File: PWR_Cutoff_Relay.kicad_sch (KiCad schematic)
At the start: 7 parts, among them K1 RAYEX-L90AS, Q1 Q_NMOS_GSD

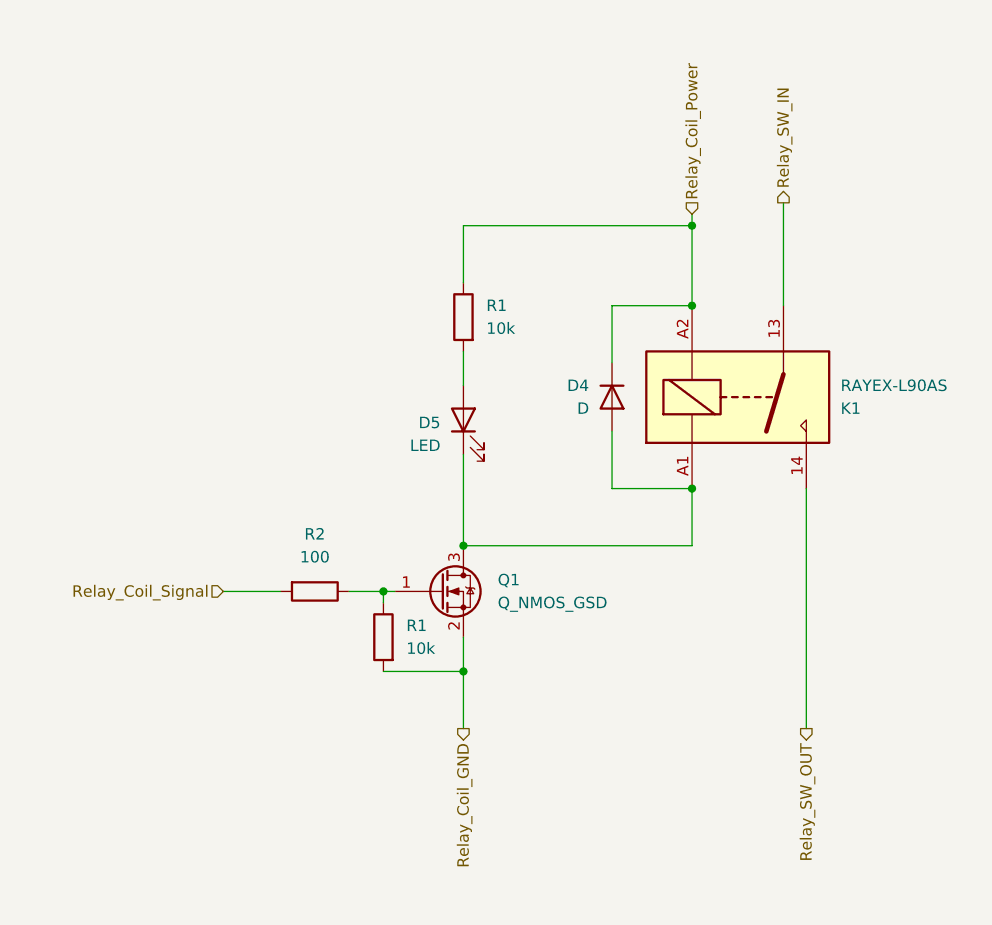
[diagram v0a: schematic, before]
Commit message: add switch, EMS & MCU
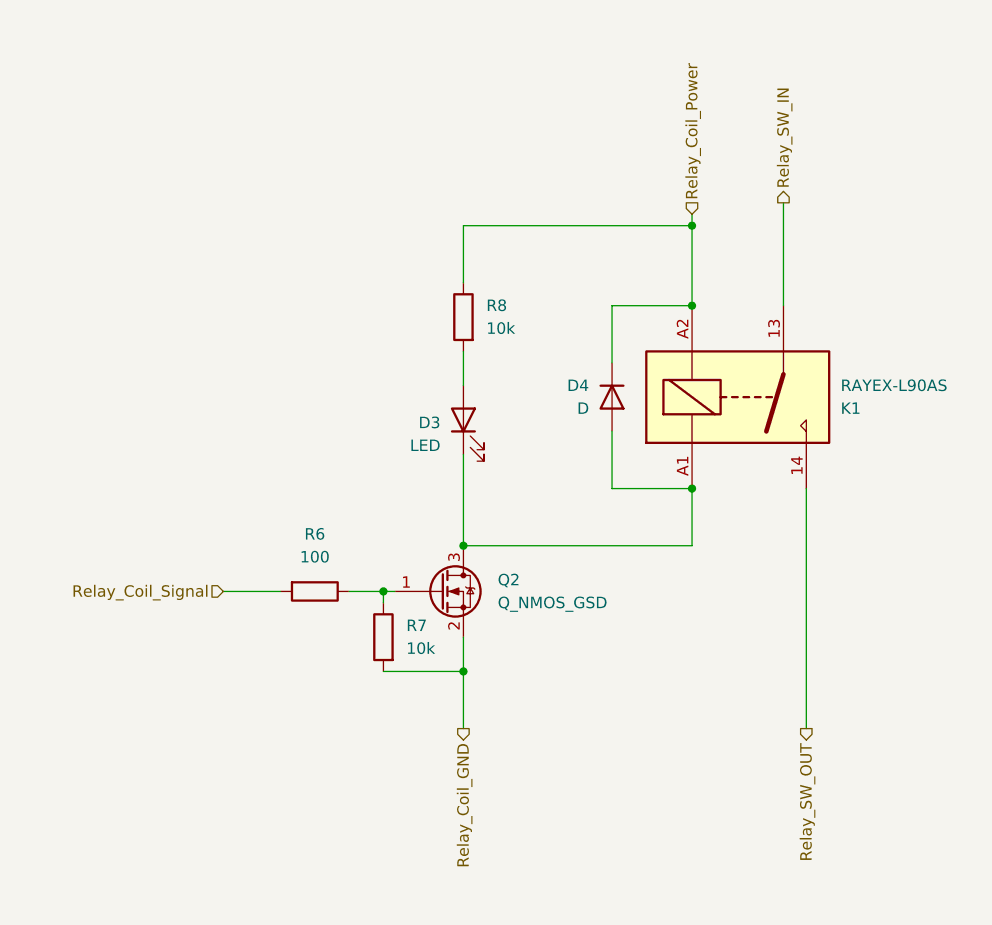
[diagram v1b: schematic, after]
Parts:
- renumbered D5 to D3, Q1 to Q2, R2 to R6, R1 to R7, R1 to R8
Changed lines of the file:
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@@
   (symbol (lib_id "Device:LED") (at 83.82 78.74 90) (unit 1)
     (in_bom yes) (on_board yes) (dnp no)
-    (property "Reference" "D5" (at 81.28 79.0575 90)
+    (property "Reference" "D3" (at 81.28 79.0575 90)
       (effects (font (size 1.27 1.27)) (justify left))
     )
@@
       (project "schematic_PWRcutoff"
         (path "/9e89b938-308a-42c1-b814-ac47b1ea682c/41c12bc5-ee22-4bb8-97ee-b610ccf60040"
-          (reference "D5") (unit 1)
+          (reference "D3") (unit 1)
         )
         (path "/9e89b938-308a-42c1-b814-ac47b1ea682c/58bca59a-b17a-426a-980f-f68acd7ebb24"
-          (reference "D7") (unit 1)
+          (reference "D5") (unit 1)
         )
       )
@@
   (symbol (lib_id "Device:R") (at 67.31 97.79 270) (unit 1)
     (in_bom yes) (on_board yes) (dnp no) (fields_autoplaced)
-    (property "Reference" "R2" (at 67.31 91.44 90)
+    (property "Reference" "R6" (at 67.31 91.44 90)
       (effects (font (size 1.27 1.27)))
     )
@@
     (instances
       (project "schematic_PWRcutoff"
-        (path "/9e89b938-308a-42c1-b814-ac47b1ea682c"
-          (reference "R2") (unit 1)
-        )
         (path "/9e89b938-308a-42c1-b814-ac47b1ea682c/41c12bc5-ee22-4bb8-97ee-b610ccf60040"
           (reference "R6") (unit 1)
@@
   (symbol (lib_id "Device:R") (at 74.93 102.87 0) (mirror y) (unit 1)
     (in_bom yes) (on_board yes) (dnp no) (fields_autoplaced)
-    (property "Reference" "R1" (at 77.47 101.6 0)
+    (property "Reference" "R7" (at 77.47 101.6 0)
       (effects (font (size 1.27 1.27)) (justify right))
     )
@@
     (instances
       (project "schematic_PWRcutoff"
-        (path "/9e89b938-308a-42c1-b814-ac47b1ea682c"
-          (reference "R1") (unit 1)
-        )
         (path "/9e89b938-308a-42c1-b814-ac47b1ea682c/41c12bc5-ee22-4bb8-97ee-b610ccf60040"
           (reference "R7") (unit 1)
@@
   (symbol (lib_id "Device:R") (at 83.82 67.31 0) (mirror y) (unit 1)
     (in_bom yes) (on_board yes) (dnp no) (fields_autoplaced)
-    (property "Reference" "R1" (at 86.36 66.04 0)
+    (property "Reference" "R8" (at 86.36 66.04 0)
       (effects (font (size 1.27 1.27)) (justify right))
     )
@@
     (instances
       (project "schematic_PWRcutoff"
-        (path "/9e89b938-308a-42c1-b814-ac47b1ea682c"
-          (reference "R1") (unit 1)
-        )
         (path "/9e89b938-308a-42c1-b814-ac47b1ea682c/41c12bc5-ee22-4bb8-97ee-b610ccf60040"
-          (reference "R5") (unit 1)
+          (reference "R8") (unit 1)
         )
         (path "/9e89b938-308a-42c1-b814-ac47b1ea682c/58bca59a-b17a-426a-980f-f68acd7ebb24"
-          (reference "R8") (unit 1)
+          (reference "R11") (unit 1)
         )
       )
@@
   (symbol (lib_id "Device:Q_NMOS_GSD") (at 81.28 97.79 0) (unit 1)
     (in_bom yes) (on_board yes) (dnp no) (fields_autoplaced)
-    (property "Reference" "Q1" (at 87.63 96.52 0)
+    (property "Reference" "Q2" (at 87.63 96.52 0)
       (effects (font (size 1.27 1.27)) (justify left))
     )
@@
       (project "schematic_PWRcutoff"
         (path "/9e89b938-308a-42c1-b814-ac47b1ea682c/41c12bc5-ee22-4bb8-97ee-b610ccf60040"
-          (reference "Q1") (unit 1)
+          (reference "Q2") (unit 1)
         )
         (path "/9e89b938-308a-42c1-b814-ac47b1ea682c/58bca59a-b17a-426a-980f-f68acd7ebb24"
-          (reference "Q2") (unit 1)
+          (reference "Q3") (unit 1)
         )
       )
